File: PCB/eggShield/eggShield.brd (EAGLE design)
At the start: 100 x 80 mm, 30 parts, among them IC10 MCP601OT, IC6 MCP601OT, IC7 MCP601OT

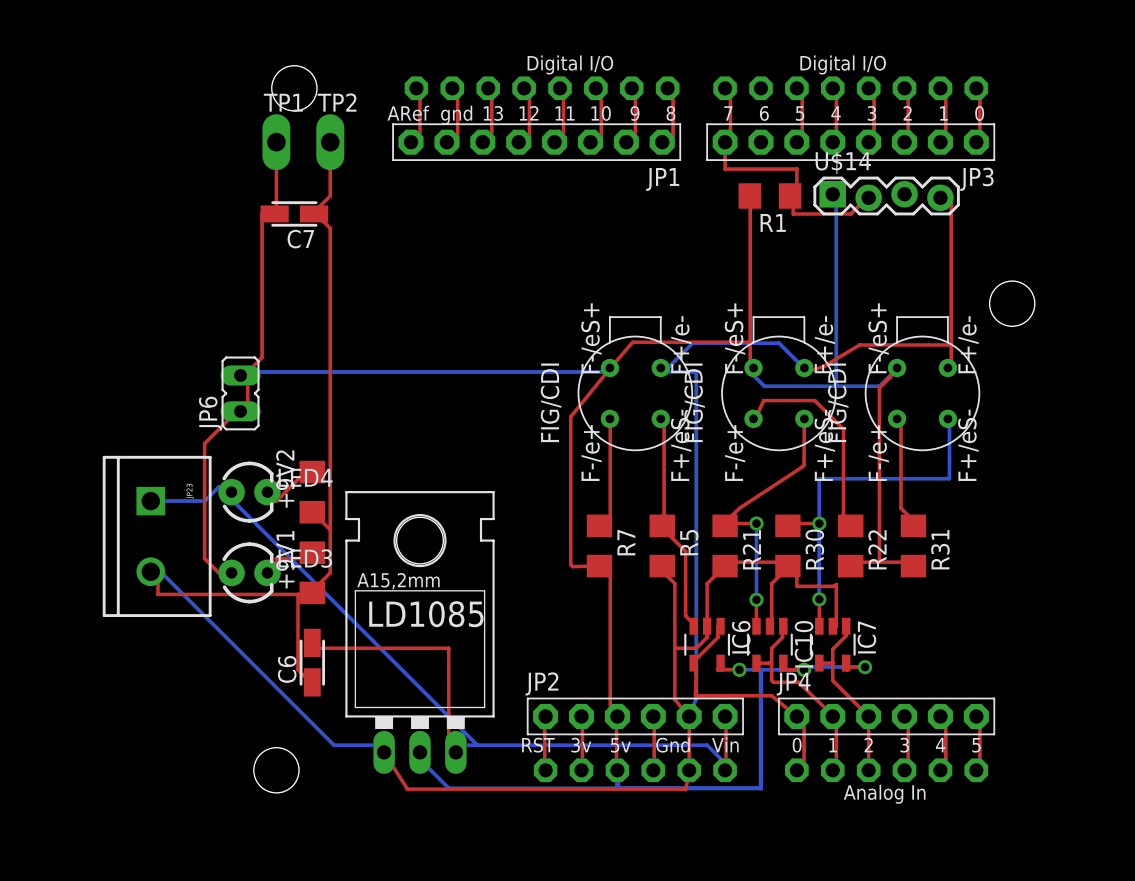
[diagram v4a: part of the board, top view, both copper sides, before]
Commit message: updated sensor circuit, removed unneeded compnts
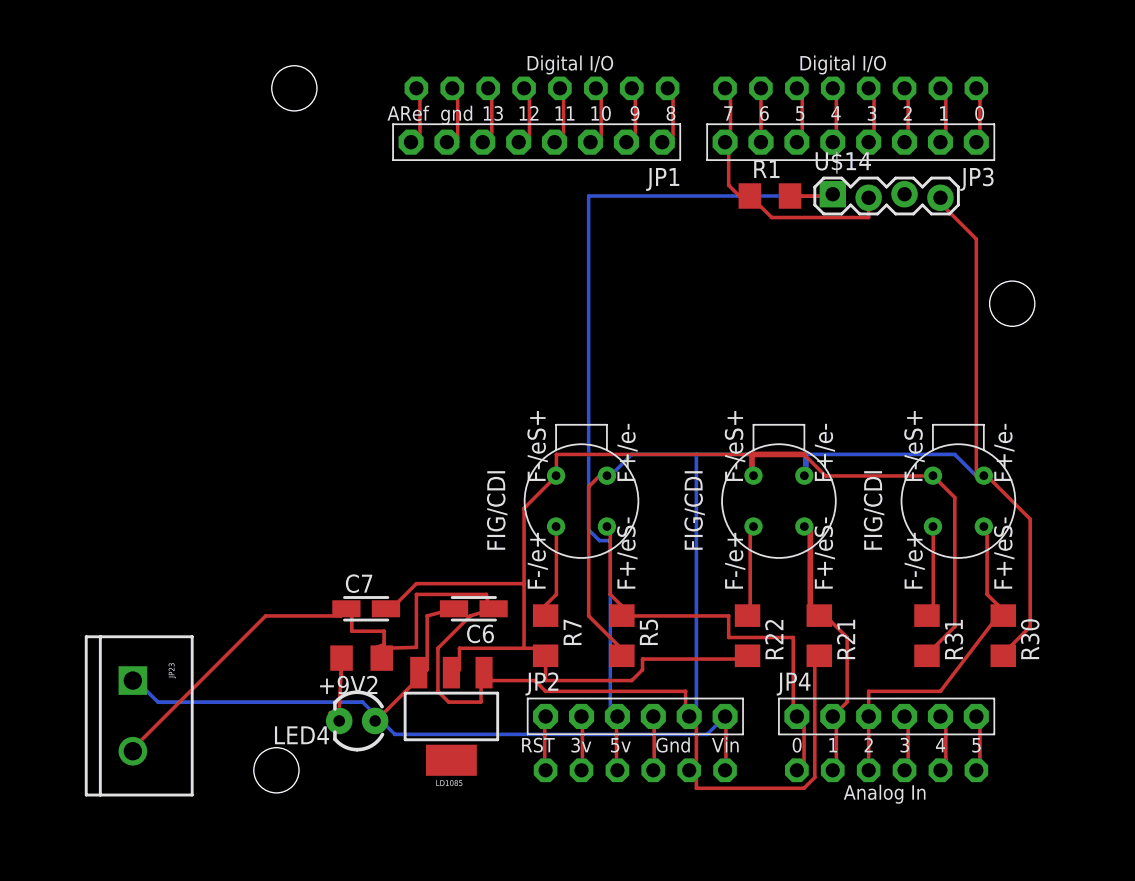
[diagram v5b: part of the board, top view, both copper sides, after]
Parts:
- removed +9V1: 500 ohm, rcl:R1206
- removed IC10, IC6, IC7: MCP601OT, linear:SOT23-5
- removed JP6: (no value), jumper:JP1
- removed LED3: (no value), SparkFun:LED3MM
- removed TP1, TP2: TPPAD1-13Y, testpad:P1-13Y
- LD1085: value (none) -> V_REG_317SMD; device v-reg:TO220L1 -> SparkFun:SOT223
- moved C7 28.4 mm to (36.8, 27.9), turned to 0 degrees
- moved LED4 17.9 mm to (36.2, 20.0), turned to 180 degrees
- moved R30 16.5 mm to (81.9, 26.0)
- moved JP23 12.8 mm to (20.3, 22.9)
- moved +9V2 12.3 mm to (36.5, 24.4), turned to 180 degrees
- moved C6 12.0 mm to (44.5, 27.9), turned to 180 degrees
- moved R22 9.68 mm to (63.8, 26.0)
- moved R21 9.21 mm to (68.9, 26.0)
- moved NO2 8.52 mm to (52.1, 35.6)
- moved U$9 8.03 mm to (78.7, 35.6)
- moved U$13 7.62 mm to (66.0, 35.6)
- moved R7 7.41 mm to (49.5, 26.0)
- moved R5 6.96 mm to (54.9, 26.0)
- moved R31 6.42 mm to (76.5, 26.0)
- moved LD1085 2.56 mm to (42.9, 20.3), turned to 180 degrees
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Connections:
- removed net GND: +9V1.1, +9V2.1, C6.-, C7.-, IC10.2, IC6.2, IC7.2, JP2.5, JP23.2, LD1085.1, NO2.FIGV+/E2V-, R21.2, R30.2, R5.2, TP2.TP, U$13.FIGV+/E2V-, U$14.GND, U$2.GND1, U$9.FIGV+/E2V-
- removed net N$19: +9V1.2, LED3.K
- removed net N$48: IC10.1, IC10.4, JP4.2, U$2.A1
- removed net N$52: IC6.1, IC6.4, JP4.1, U$2.A0
- removed net N$9: IC7.1, IC7.4, JP4.3, U$2.A2
- new net +5V: JP2.3, R1.2, U$14.VDD, U$2.5V
- new net 1.8: +9V2.1, C6.-, C7.-, JP2.5, JP23.2, LD1085.1, NO2.FIGV+/E2V-, R21.2, R30.2, R5.2, U$13.FIGV+/E2V-, U$14.GND, U$2.GND1, U$9.FIGV+/E2V-
- net N$47: now also JP4.2, U$2.A1; no longer IC10.3
- net N$50: now also JP4.1, U$2.A0; no longer IC6.3
- net N$55: now also JP4.3, U$2.A2; no longer IC7.3
- net V+: no longer IC10.5, IC6.5, IC7.5, JP2.3, JP6.1, JP6.2, LED3.A, R1.2, TP1.TP, U$14.VDD, U$2.5V
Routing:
- net GND: track 206.4 -> 0.00 mm
- net 1.8: track 0.00 -> 191.6 mm
- net V+: track 213.8 -> 97.6 mm, vias 3 -> 0
- net +5V: track 0.00 -> 62.4 mm
- net N$52: track 17.8 -> 0.00 mm
- net N$48: track 14.8 -> 0.00 mm
- net +9V: track 73.7 -> 59.2 mm
- net N$50: track 16.0 -> 30.4 mm
- net N$9: track 12.6 -> 0.00 mm
- net N$38: track 15.2 -> 6.42 mm
- net N$19: track 4.33 -> 0.00 mm
- net N$5: track 0.00 -> 3.81 mm
- net N$43: track 8.94 -> 6.62 mm
- net N$55: track 26.3 -> 24.6 mm, vias 2 -> 0
- net N$24: track 4.28 -> 5.91 mm
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
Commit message: cleaned power circuit
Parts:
- moved C6 10.9 mm to (42.9, 17.1)
- moved C7 4.45 mm to (32.4, 27.9)
- moved +9V2 3.81 mm to (32.7, 24.4)
- moved LD1085 3.81 mm to (42.9, 24.1)
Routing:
- net +9V: track 59.2 -> 65.8 mm
- net 1.8: track 191.6 -> 186.3 mm, vias 0 -> 1
- net V+: track 97.6 -> 101.2 mm
- net N$24: track 5.91 -> 6.71 mm

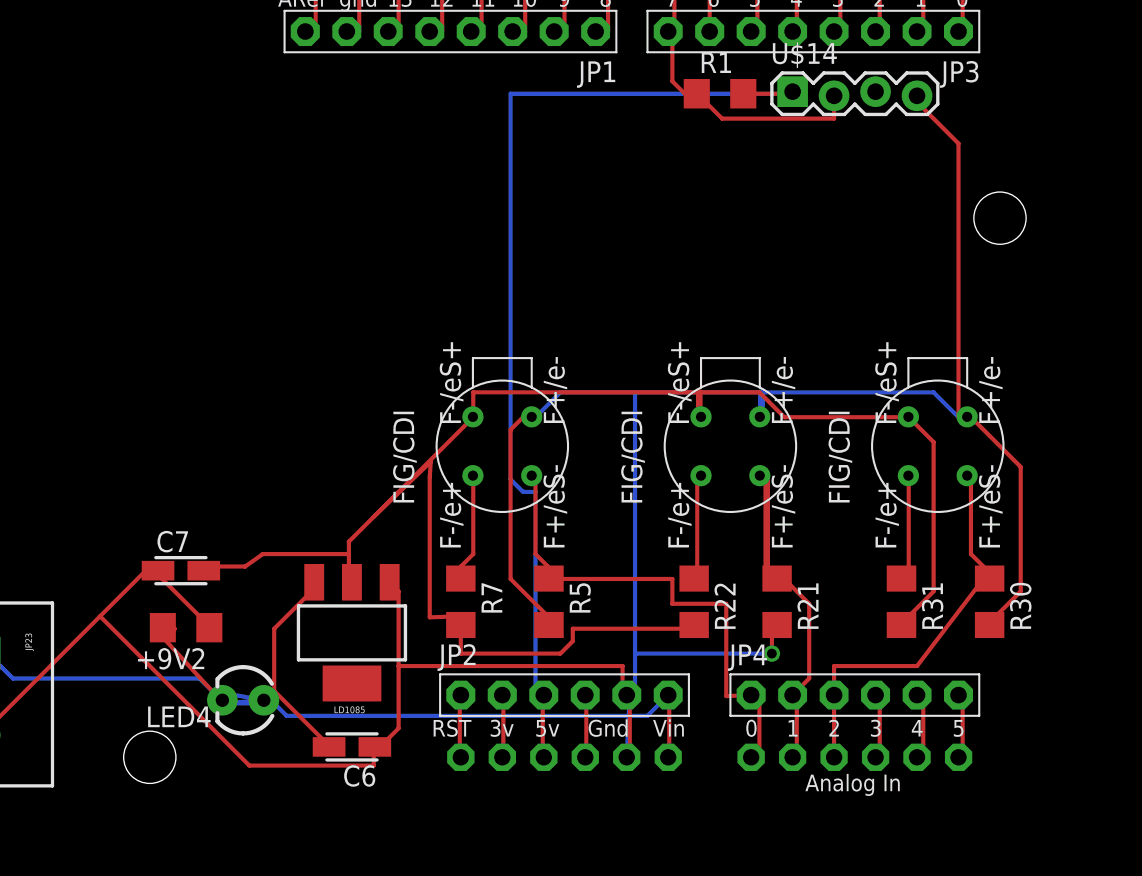
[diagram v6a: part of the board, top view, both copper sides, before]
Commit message: sensor update, needs i2c bus
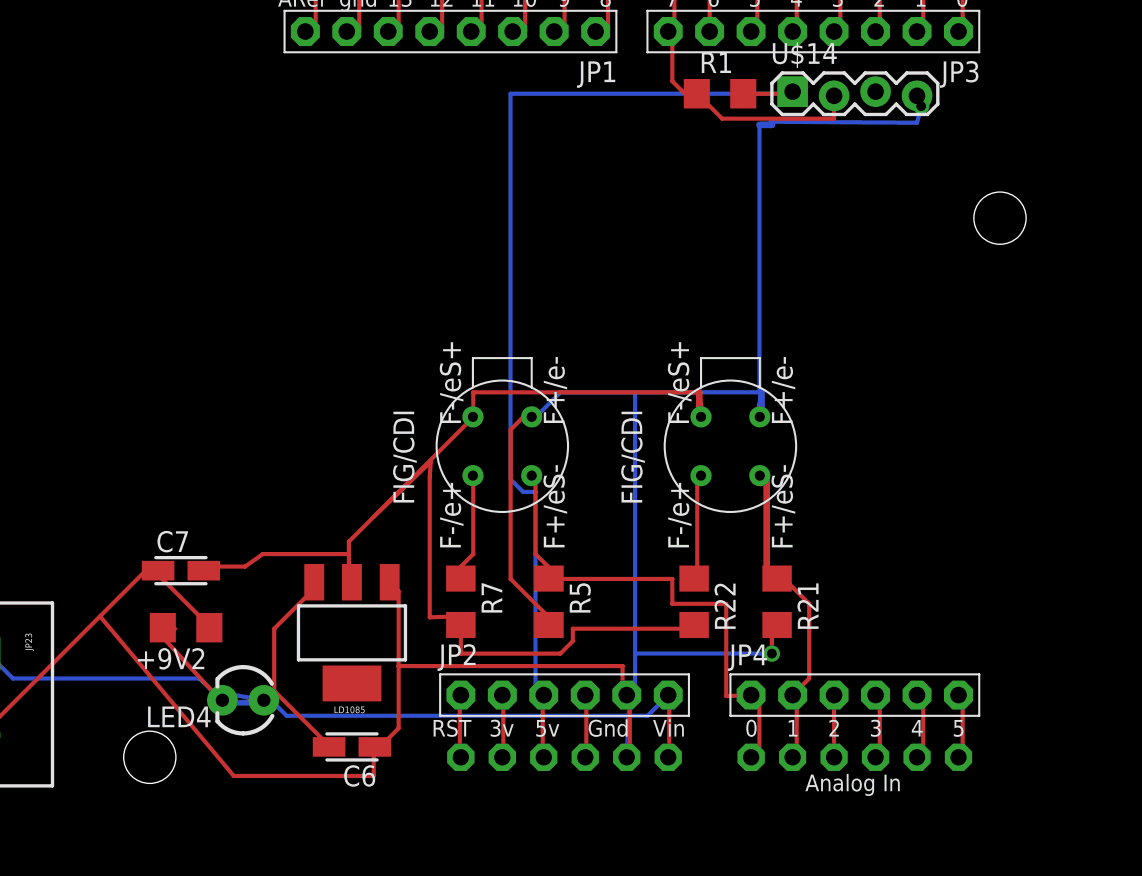
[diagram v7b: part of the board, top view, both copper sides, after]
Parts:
- removed R30: 220k, rcl:R1206
- removed R31: 60 ohm, rcl:R1206
- removed U$9: E2V Ozone, ricardo:SR-4
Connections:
- removed net N$45: R31.1, U$9.FIGSIG/E2VH+
- net 1.8: no longer R30.2, U$9.FIGV+/E2V-
- net N$55: no longer R30.1, U$9.FIGV+/E2VSIG
- net V+: no longer R31.2, U$9.FIGG/E2VS+
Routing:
- net V+: track 101.2 -> 75.5 mm
- net N$55: track 24.6 -> 4.68 mm
- net 1.8: track 186.3 -> 169.6 mm, vias 1 -> 2
- net N$45: track 6.43 -> 0.00 mm
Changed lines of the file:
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@@
 <element name="R5" library="rcl" package="R1206" value="220k" x="54.9275" y="26.035" rot="R270"/>
 <element name="R7" library="rcl" package="R1206" value="34 ohm" x="49.53" y="26.035" rot="R270"/>
-<element name="U$9" library="ricardo" package="SR-4" value="E2V Ozone" x="78.74" y="35.56" rot="R90"/>
-<element name="R30" library="rcl" package="R1206" value="220k" x="81.915" y="26.035" rot="R270"/>
-<element name="R31" library="rcl" package="R1206" value="60 ohm" x="76.5175" y="26.035" rot="R270"/>
 <element name="JP23" library="SparkFun" package="SCREWTERMINAL-5MM-2" value="Screw Terminal" x="20.32" y="22.86" rot="R270"/>
 <element name="R1" library="rcl" package="R1206" value="10k" x="65.405" y="57.15"/>
@@
 <contactref element="NO2" pad="FIGV+/E2V-"/>
 <contactref element="R5" pad="2"/>
-<contactref element="U$9" pad="FIGV+/E2V-"/>
-<contactref element="R30" pad="2"/>
 <contactref element="JP23" pad="2"/>
 <contactref element="JP2" pad="5"/>
@@
 <wire x1="68.58" y1="24.384" x2="68.8975" y2="24.613" width="0.254" layer="1"/>
 <wire x1="59.8805" y1="20.447" x2="59.69" y2="16.51" width="0.254" layer="16"/>
-<wire x1="83.82" y1="26.67" x2="82.296" y2="25.146" width="0.254" layer="1"/>
-<wire x1="83.82" y1="34.29" x2="83.82" y2="26.67" width="0.254" layer="1"/>
-<wire x1="80.772" y1="37.338" x2="83.82" y2="34.29" width="0.254" layer="1"/>
-<wire x1="82.296" y1="25.146" x2="81.915" y2="24.613" width="0.254" layer="1"/>
-<wire x1="80.772" y1="37.338" x2="80.54" y2="37.36" width="0.254" layer="1"/>
-<wire x1="80.01" y1="54.102" x2="77.724" y2="56.388" width="0.254" layer="1"/>
-<wire x1="80.01" y1="37.338" x2="80.01" y2="54.102" width="0.254" layer="1"/>
+<wire x1="77.47" y1="55.372" x2="77.724" y2="56.388" width="0.254" layer="16"/>
+<wire x1="68.58" y1="55.4355" x2="77.47" y2="55.372" width="0.254" layer="16"/>
 <wire x1="77.724" y1="56.388" x2="77.47" y2="57.023" width="0.254" layer="1"/>
-<wire x1="80.01" y1="37.338" x2="80.54" y2="37.36" width="0.254" layer="1"/>
 <wire x1="55.626" y1="38.862" x2="54.102" y2="37.338" width="0.254" layer="16"/>
-<wire x1="78.486" y1="38.862" x2="67.945" y2="38.862" width="0.254" layer="16"/>
-<wire x1="67.945" y1="38.862" x2="60.198" y2="38.862" width="0.254" layer="16"/>
+<wire x1="67.691" y1="37.2745" x2="67.945" y2="38.862" width="0.254" layer="16"/>
+<wire x1="67.945" y1="38.862" x2="67.818" y2="38.862" width="0.254" layer="16"/>
+<wire x1="67.818" y1="38.862" x2="60.198" y2="38.862" width="0.254" layer="16"/>
 <wire x1="60.198" y1="38.862" x2="55.626" y2="38.862" width="0.254" layer="16"/>
-<wire x1="80.01" y1="37.338" x2="78.486" y2="38.862" width="0.254" layer="16"/>
+<wire x1="67.945" y1="38.9255" x2="67.691" y2="37.2745" width="0.254" layer="16"/>
 <wire x1="54.102" y1="37.338" x2="53.87" y2="37.36" width="0.254" layer="16"/>
-<wire x1="80.01" y1="37.338" x2="80.54" y2="37.36" width="0.254" layer="16"/>
 <wire x1="60.198" y1="38.862" x2="60.198" y2="22.86" width="0.254" layer="16"/>
 <wire x1="60.198" y1="22.86" x2="60.198" y2="20.574" width="0.254" layer="16"/>
@@
 <wire x1="20.574" y1="18.288" x2="20.32" y2="17.86" width="0.254" layer="1"/>
 <wire x1="30.48" y1="28.194" x2="30.985" y2="27.94" width="0.254" layer="1"/>
-<wire x1="36.576" y1="16.002" x2="27.432" y2="25.146" width="0.254" layer="1"/>
-<wire x1="44.196" y1="16.002" x2="36.576" y2="16.002" width="0.254" layer="1"/>
-<wire x1="44.196" y1="16.764" x2="44.196" y2="16.002" width="0.254" layer="1"/>
+<wire x1="35.6235" y1="15.367" x2="27.432" y2="25.146" width="0.254" layer="1"/>
+<wire x1="44.196" y1="15.367" x2="35.6235" y2="15.367" width="0.254" layer="1"/>
+<wire x1="44.196" y1="16.764" x2="44.196" y2="15.367" width="0.254" layer="1"/>
 <wire x1="44.196" y1="16.764" x2="44.2625" y2="17.145" width="0.254" layer="1"/>
 <wire x1="31.242" y1="27.432" x2="33.528" y2="25.146" width="0.254" layer="1"/>
@@
 <wire x1="31.242" y1="27.432" x2="30.985" y2="27.94" width="0.254" layer="1"/>
 <via x="68.58" y="22.86" extent="1-16" drill="0.6" shape="square"/>
+<via x="77.724" y="56.388" extent="1-16" drill="0.6" shape="square"/>
+<wire x1="68.58" y1="55.4355" x2="68.58" y2="55.245" width="0.4064" layer="16"/>
+<wire x1="67.818" y1="55.245" x2="68.58" y2="55.245" width="0.4064" layer="16"/>
+<wire x1="67.818" y1="38.862" x2="67.818" y2="55.245" width="0.254" layer="16"/>
 </signal>
 <signal name="V+">
@@
 <contactref element="R7" pad="2"/>
 <contactref element="NO2" pad="FIGG/E2VS+"/>
-<contactref element="R31" pad="2"/>
-<contactref element="U$9" pad="FIGG/E2VS+"/>
 <contactref element="LD1085" pad="2"/>
 <contactref element="C7" pad="+"/>
@@
 <wire x1="49.53" y1="24.613" x2="49.53" y2="22.86" width="0.254" layer="1"/>
 <wire x1="63.246" y1="24.384" x2="63.8175" y2="24.613" width="0.254" layer="1"/>
-<wire x1="78.486" y1="26.67" x2="76.962" y2="25.146" width="0.254" layer="1"/>
-<wire x1="78.486" y1="35.814" x2="78.486" y2="26.67" width="0.254" layer="1"/>
-<wire x1="76.962" y1="37.338" x2="78.486" y2="35.814" width="0.254" layer="1"/>
-<wire x1="76.962" y1="25.146" x2="76.5175" y2="24.613" width="0.254" layer="1"/>
+<wire x1="64.1985" y1="37.465" x2="64.262" y2="37.211" width="0.254" layer="1"/>
+<wire x1="64.1985" y1="37.4015" x2="64.1985" y2="37.465" width="0.254" layer="1"/>
+<wire x1="64.262" y1="37.338" x2="64.1985" y2="37.4015" width="0.254" layer="1"/>
 <wire x1="36.322" y1="28.194" x2="34.29" y2="28.194" width="0.254" layer="1"/>
 <wire x1="37.4015" y1="28.956" x2="36.322" y2="28.194" width="0.254" layer="1"/>
@@
 <wire x1="44.196" y1="31.242" x2="50.292" y2="37.338" width="0.254" layer="1"/>
 <wire x1="42.672" y1="28.956" x2="42.672" y2="29.718" width="0.254" layer="1"/>
-<wire x1="69.342" y1="37.338" x2="76.962" y2="37.338" width="0.254" layer="1"/>
-<wire x1="67.818" y1="38.862" x2="69.342" y2="37.338" width="0.254" layer="1"/>
+<wire x1="64.3255" y1="37.592" x2="64.262" y2="37.338" width="0.254" layer="1"/>
 <wire x1="50.292" y1="38.862" x2="64.135" y2="38.862" width="0.254" layer="1"/>
-<wire x1="64.135" y1="38.862" x2="67.818" y2="38.862" width="0.254" layer="1"/>
+<wire x1="64.135" y1="38.862" x2="64.3255" y2="37.592" width="0.254" layer="1"/>
 <wire x1="50.292" y1="37.338" x2="50.292" y2="38.862" width="0.254" layer="1"/>
-<wire x1="76.962" y1="37.338" x2="76.94" y2="37.36" width="0.254" layer="1"/>
 <wire x1="50.292" y1="37.338" x2="50.27" y2="37.36" width="0.254" layer="1"/>
 <wire x1="47.6885" y1="34.6075" x2="47.625" y2="33.655" width="0.254" layer="1"/>
@@
 <wire x1="50.292" y1="33.528" x2="50.27" y2="33.76" width="0.254" layer="1"/>
 </signal>
-<signal name="N$45">
-<contactref element="U$9" pad="FIGSIG/E2VH+"/>
-<contactref element="R31" pad="1"/>
-<wire x1="76.962" y1="33.528" x2="76.962" y2="28.194" width="0.254" layer="1"/>
-<wire x1="76.962" y1="28.194" x2="76.5175" y2="27.457" width="0.254" layer="1"/>
-<wire x1="76.962" y1="33.528" x2="76.94" y2="33.76" width="0.254" layer="1"/>
-</signal>
 <signal name="A3">
 <contactref element="U$14" pad="DATA"/>
@@
 </signal>
 <signal name="N$55">
-<contactref element="U$9" pad="FIGV+/E2VSIG"/>
-<contactref element="R30" pad="1"/>
 <contactref element="JP4" pad="3"/>
 <contactref element="U$2" pad="A2"/>
 <wire x1="72.39" y1="20.32" x2="72.39" y2="16.51" width="0.254" layer="1"/>
-<wire x1="80.772" y1="28.956" x2="81.534" y2="28.194" width="0.254" layer="1"/>
-<wire x1="80.772" y1="33.528" x2="80.772" y2="28.956" width="0.254" layer="1"/>
-<wire x1="81.534" y1="28.194" x2="81.915" y2="27.457" width="0.254" layer="1"/>
-<wire x1="80.772" y1="33.528" x2="80.54" y2="33.76" width="0.254" layer="1"/>
-<wire x1="77.47" y1="22.098" x2="81.534" y2="27.432" width="0.254" layer="1"/>
-<wire x1="72.39" y1="22.098" x2="77.47" y2="22.098" width="0.254" layer="1"/>
-<wire x1="72.39" y1="20.32" x2="72.39" y2="22.098" width="0.254" layer="1"/>
-<wire x1="81.534" y1="27.432" x2="81.915" y2="27.457" width="0.254" layer="1"/>
+<wire x1="72.39" y1="20.828" x2="72.644" y2="21.082" width="0.254" layer="1"/>
+<wire x1="72.39" y1="20.32" x2="72.39" y2="20.828" width="0.254" layer="1"/>
 </signal>
 <signal name="N$47">

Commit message: cleaned up
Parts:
- moved U$13 21.6 mm to (49.5, 21.6)
- moved JP1 21.6 mm to (32.4, 47.0)
- moved JP2 21.6 mm to (39.4, 6.35)
- moved JP3 21.6 mm to (54.6, 47.0)
- moved R22 21.6 mm to (47.3, 12.1)
- moved R5 21.6 mm to (38.4, 12.1)
- moved +9V2 21.6 mm to (16.2, 10.5)
- moved JP23 21.6 mm to (3.81, 8.89)
- moved LED4 21.6 mm to (19.7, 6.03)
- moved U$2 21.6 mm to (0.00, 0.00)
- moved C6 21.6 mm to (26.4, 3.17)
- moved C7 21.6 mm to (15.9, 14.0)
- moved JP4 21.6 mm to (57.1, 6.35)
- moved LD1085 21.6 mm to (26.4, 10.2)
- moved NO2 21.6 mm to (35.6, 21.6)
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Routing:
- net V+: track 75.5 -> 74.5 mm
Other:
- board size 100 x 80 mm -> 68.6 x 53.3 mm
- board text added: "Air Quality Egg"
- board text added: "Sensor Shield v01"
